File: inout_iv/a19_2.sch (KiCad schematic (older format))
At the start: 34 parts, among them U19019 74HC4002, U19030 74HC27, U19032 74HC02, U19033 74HC04, U19034 74HC02, U19035 74HC02, U19036 74HC04, U19037 74HC02, U19038 74HC02, U19039 74HC02, U19040 74HC02, U19041 74HC02, U19042 74HC02, U19043 74HC02, U19044 74HC27, U19045 74HC02, U19046 74HC02, U19047 74HC04, U19048 74HC02, U19049 74HC02, U19050 74HC02, U19051 74HC02, U19052 74HC02, U19053 74HC27, U19054 74HC04, U19055 74HC27, U19056 74HC02, U19057 74HC02, U19058 74HC27, U19059 74HC27, U19060 74HC02, U19061 74HC02, U19062 74HC02, U19063 74HC27

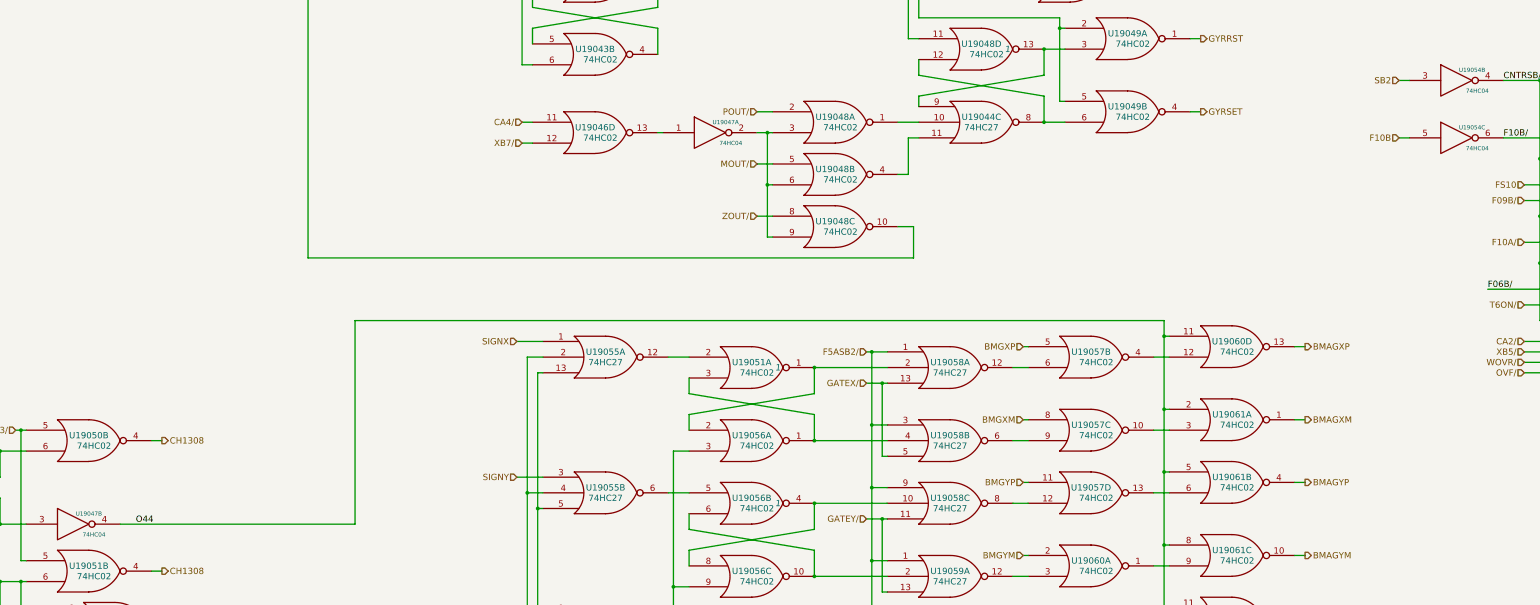
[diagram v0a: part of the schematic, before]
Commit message: Tied in Inout IV and renamed MONPCH to the original MON+CH
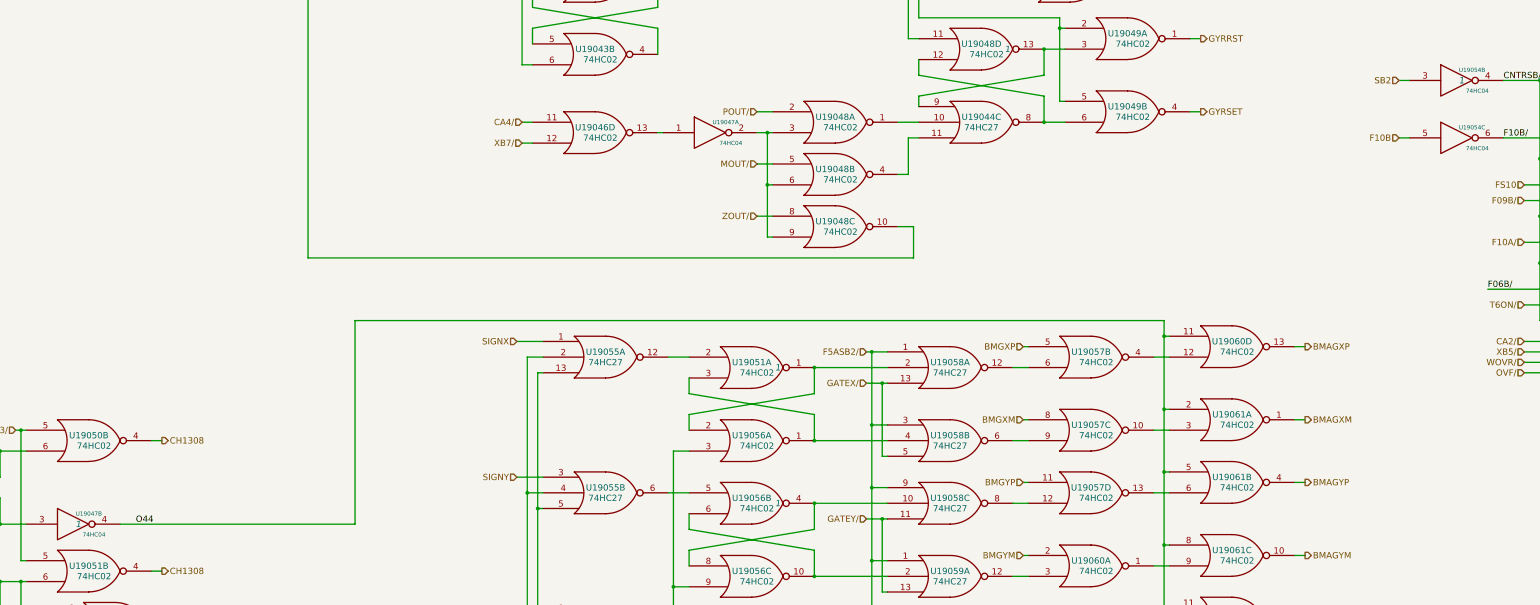
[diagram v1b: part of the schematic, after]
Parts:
- U19047, U19054: Initial (none) -> 1
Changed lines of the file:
@@
 F 2 "" H 5400 11550 60  0000 C CNN
 F 3 "" H 5400 11550 60  0000 C CNN
+F 4 "1" H 5450 11550 60  0000 C CIN "Initial"
 	2    5400 11550
 	1    0    0    -1
@@
 F 2 "" H 18650 7300 60  0000 C CNN
 F 3 "" H 18650 7300 60  0000 C CNN
+F 4 "1" H 18700 7300 60  0000 C CIN "Initial"
 	2    18650 7300
 	1    0    0    -1

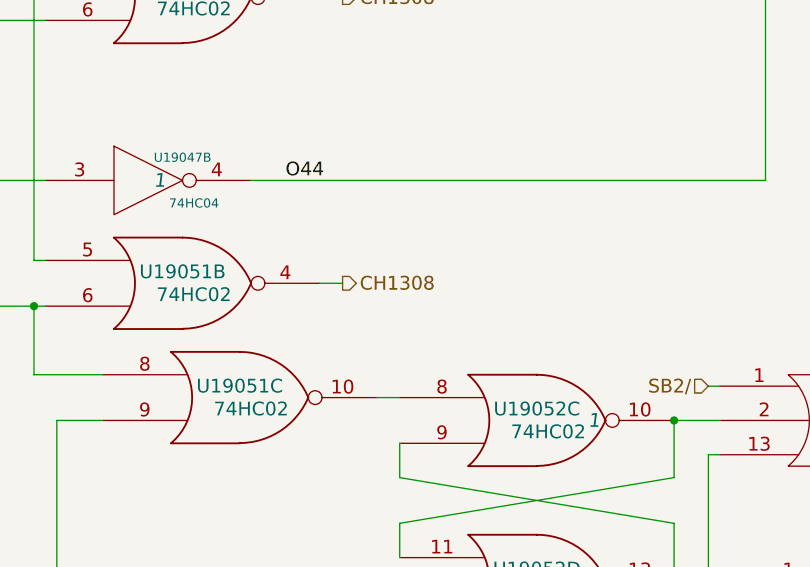
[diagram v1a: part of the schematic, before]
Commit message: Added and tied in Inout VI. Pulled in all PIPA related things. Almost there!
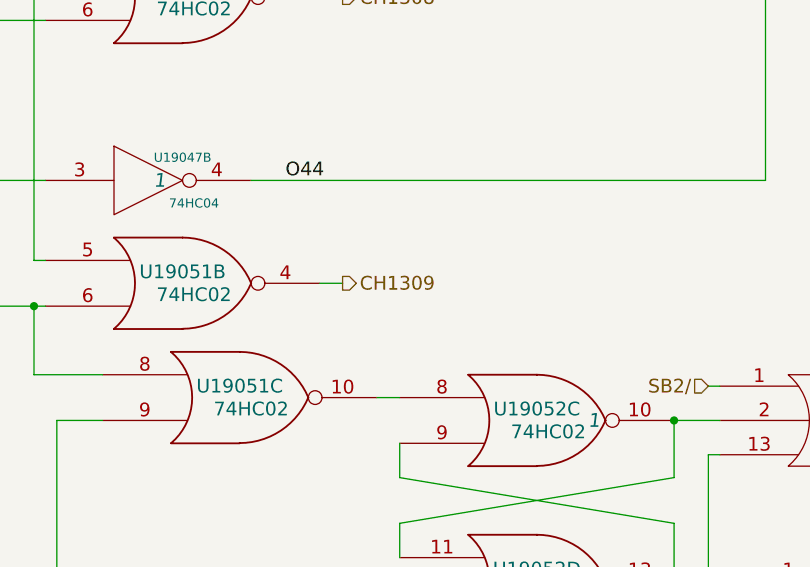
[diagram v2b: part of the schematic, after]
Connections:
- net CH1308: no longer U19051.4
- new net CH1309: U19051.4
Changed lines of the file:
@@
 $EndComp
 Text HLabel 6250 12000 2    60   Output ~ 0
-CH1308
+CH1309
 $Comp
 L 74HC02 U19051

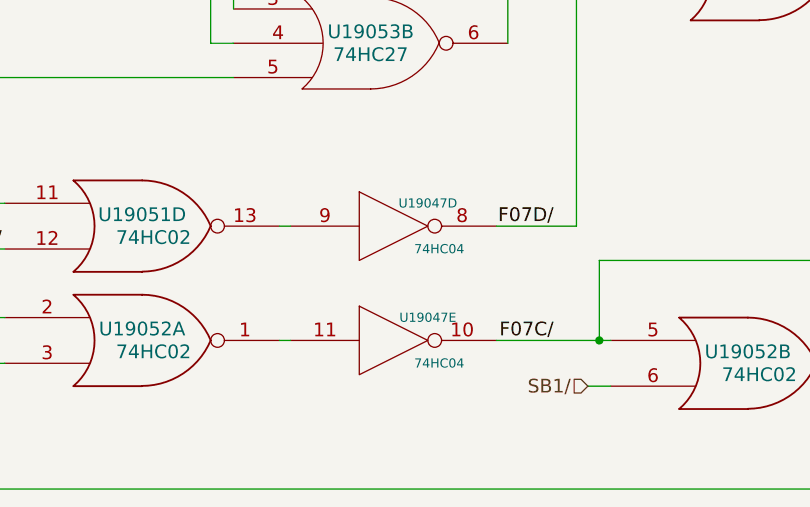
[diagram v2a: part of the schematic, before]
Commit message: Lots of initial conditions, some missed gates, and some wiring fixes
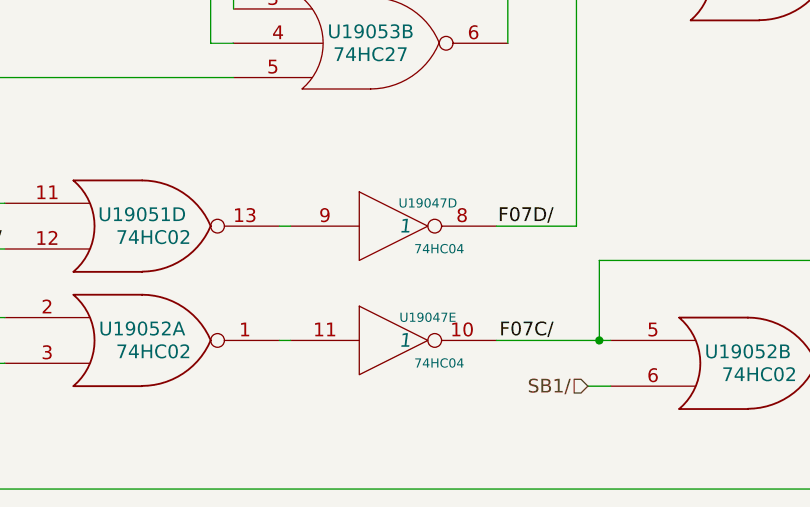
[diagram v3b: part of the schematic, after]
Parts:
- U19047: Initial (none) -> 1
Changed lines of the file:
@@
 F 2 "" H 4200 13600 60  0000 C CNN
 F 3 "" H 4200 13600 60  0000 C CNN
+F 4 "1" H 4250 13600 60  0000 C CIN "Initial"
 	4    4200 13600
 	1    0    0    -1
@@
 F 2 "" H 4200 14100 60  0000 C CNN
 F 3 "" H 4200 14100 60  0000 C CNN
+F 4 "1" H 4250 14100 60  0000 C CIN "Initial"
 	5    4200 14100
 	1    0    0    -1

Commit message: Fixed not->1-input nor in the rest of the modules.
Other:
- moved on the sheet: U19019B, U19033E, U19033F, U19036A, U19036B, U19036C, U19036D, U19036E, U19036F, U19045B, U19045C, U19045D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

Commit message: This adds fixes to the schematics for changes identified in comparing against the independent AGC schematics in the "schematics" branch of the main Virtual AGC repository.  Changes include:  Topological (but not logical) fixes to the DKCTR4,5,4/,5/ signals in the inout_v schematic. Wiring fix (incorrect signal sources for 5 gates) in inout_iv. Fixed incorrect signal source (including MGOJAM output polarity) for one gate in timer.  Fixed incorrect topology (but not logic) for 3 output signals in service_gates. Fixed backplane signal source (MYCLMP incorrectly used everywhere in place of the correct STRT2) in memory_timing_addressing.  ROPER, ROPES, ROPET had incorrectly omitted STRT2 as an input signal in four_bit_2. A couple of  internal nets local to sheets were also renamed due to conflicts with analysis software.  None of these fixes had any measurable effect on instruction execution; Validation was passed prior to the fixes, and continues to be passed after the fixes, and the identical instruction sequence occurs in doing so.
For me, warnings about missing components from the libraries occur upon every schematic load, though
these missing components don't seem to actually be in the circuits.  I tried to make some library
changes to work around that.  My changes don't actually fix the problem, but rather than try to back
them out and redo all the testing, they're a part of this commit as well.
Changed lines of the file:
@@
 LIBS:valves
 LIBS:inout_iv-cache
-EELAYER 25 0
+EELAYER 26 0
 EELAYER END
 $Descr A2 23386 16535
@@
 Connection ~ 10700 11400
 Wire Wire Line
-	10600 9950 10600 13450
-Wire Wire Line
 	10600 12550 10750 12550
-Connection ~ 10600 13450
 Wire Wire Line
 	10600 11250 10750 11250
@@
 Text HLabel 20150 10100 0    60   Input ~ 0
 OVF/
+Wire Wire Line
+	10600 9950 10600 13300
+Connection ~ 10600 13300
 $EndSCHEMATC
